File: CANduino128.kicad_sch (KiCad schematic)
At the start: 37 parts, among them J2 Conn_01x10, U1 AVR-H128-CAN, U2 74AHC373

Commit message: Mise à niveau du pin-out avec l'autre form-factor
git-svn-id: file:///D%5C00%20-%20Dev%20&%20Calculs%5CRepoTortoiseSVN_PCB%5CCANduino128/branches/CANduino128%20-%20v3.x@95 67ddf66f-3787-a644-8df7-7746e21a92b3
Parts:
- removed D2, D22: MountingHole_Pad, Connector_Wire:SolderWire-0.5sqmm_1x01_D0.9mm_OD2.1mm, symbol Mechanical:MountingHole_Pad
- added J1: Conn_01x02, TerminalBlock_Phoenix:TerminalBlock_Phoenix_MPT-0,5-2-2.54_1x02_P2.54mm_Horizontal, symbol Connector_Generic:Conn_01x02
- added JP1: SolderJumper_2_Open, Jumper:SolderJumper-2_P1.3mm_Open_RoundedPad1.0x1.5mm, symbol Jumper:SolderJumper_2_Open
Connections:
- net +BATT: now also J1.2 (Pin_2); no longer J_Comm_0.8 (Pin_8)
- net ADR15: now also JP1.1 (A)
- net CANH: now also J_Comm_0.6 (Pin_6); no longer J_Comm_0.5 (Pin_5)
- net CANL: now also J_Comm_0.5 (Pin_5); no longer J_Comm_0.6 (Pin_6)
- net GND: now also J1.1 (Pin_1); no longer J_Comm_0.7 (Pin_7)
- net OC1A: now also BLDC2.1 (Pin_1); no longer BLDC2.4 (Pin_4)
- net OC1B: now also BLDC2.2 (Pin_2); no longer BLDC2.5 (Pin_5)
- net OC1C: now also BLDC2.3 (Pin_3); no longer BLDC2.6 (Pin_6)
- net PIN_PD2_INT2_RXD1: now also BLDC2.4 (Pin_4); no longer BLDC2.2 (Pin_2)
- net PIN_PD3_INT3_TXD1: now also BLDC2.5 (Pin_5); no longer BLDC2.3 (Pin_3)
- net PIN_PE6_INT6: now also BLDC1.5 (Pin_5); no longer BLDC1.4 (Pin_4)
- net PIN_PE7_INT7: now also BLDC1.6 (Pin_6); no longer BLDC1.5 (Pin_5)
- net SCL_INT0: now also J_Comm_0.7 (Pin_7); no longer BLDC1.6 (Pin_6)
- net SDA_INT1: now also J_Comm_0.8 (Pin_8); no longer BLDC2.1 (Pin_1)
- net T0_OC0x: now also BusISA8.20 (BCLK); no longer BusISA8.30 (OSC)
- net PIN_PE2: now reaches U1.4 (PE2-D2-AIN0)
- net PIN_PE2: now also BLDC1.4 (Pin_4)
- net ICP1 renamed PIN_PD4
- net PIN_PD4: now also BLDC2.6 (Pin_6); no longer BusISA8.20 (BCLK)
- net SysClk renamed SW_Clock
- new net CPU_CLCK: BusISA8.30 (OSC), JP1.2 (B)
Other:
- moved on the sheet: BLDC2, CAN_RX_1, D25, KiCad0, OpenHW1, Pad_SCL1, Pad_SDA1, R_SCL1, R_SDA1

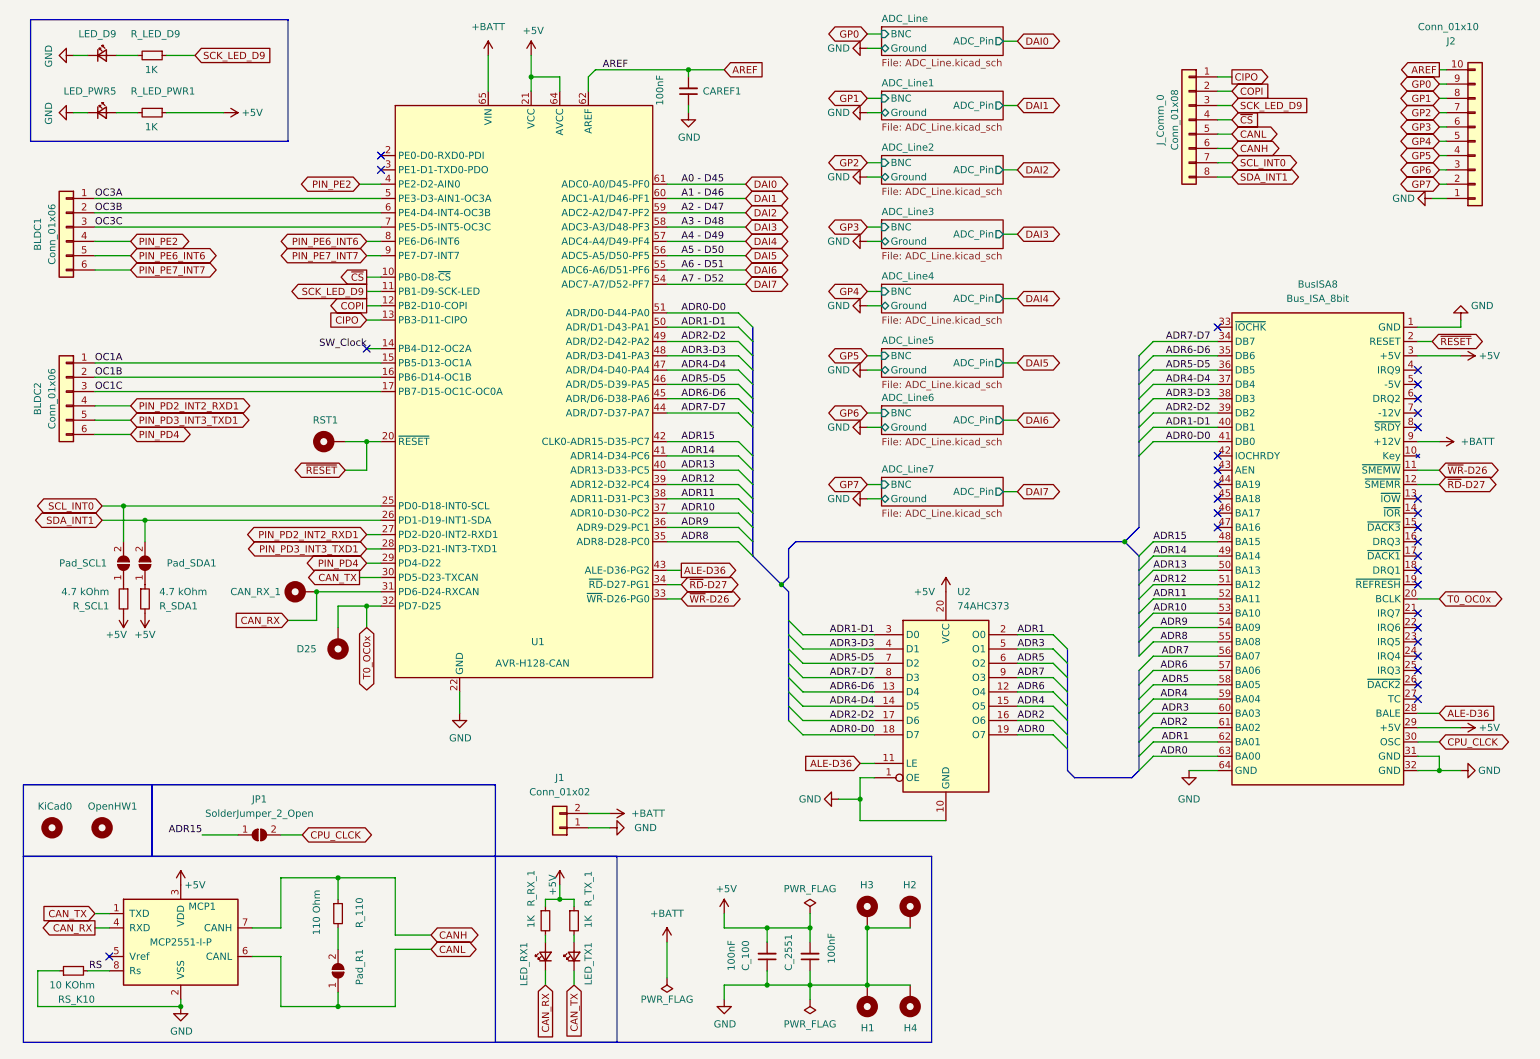
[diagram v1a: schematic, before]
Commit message: Houlà y'a eu du taf ! - fin MAJ pin-out iso v4.0a - ajout demux CD4555 pour lignes DRQ1/2/3 sur le connecteur ISA8 - pifiou ! les modifs de routages
git-svn-id: file:///D%5C00%20-%20Dev%20&%20Calculs%5CRepoTortoiseSVN_PCB%5CCANduino128/branches/CANduino128%20-%20v3.x@96 67ddf66f-3787-a644-8df7-7746e21a92b3
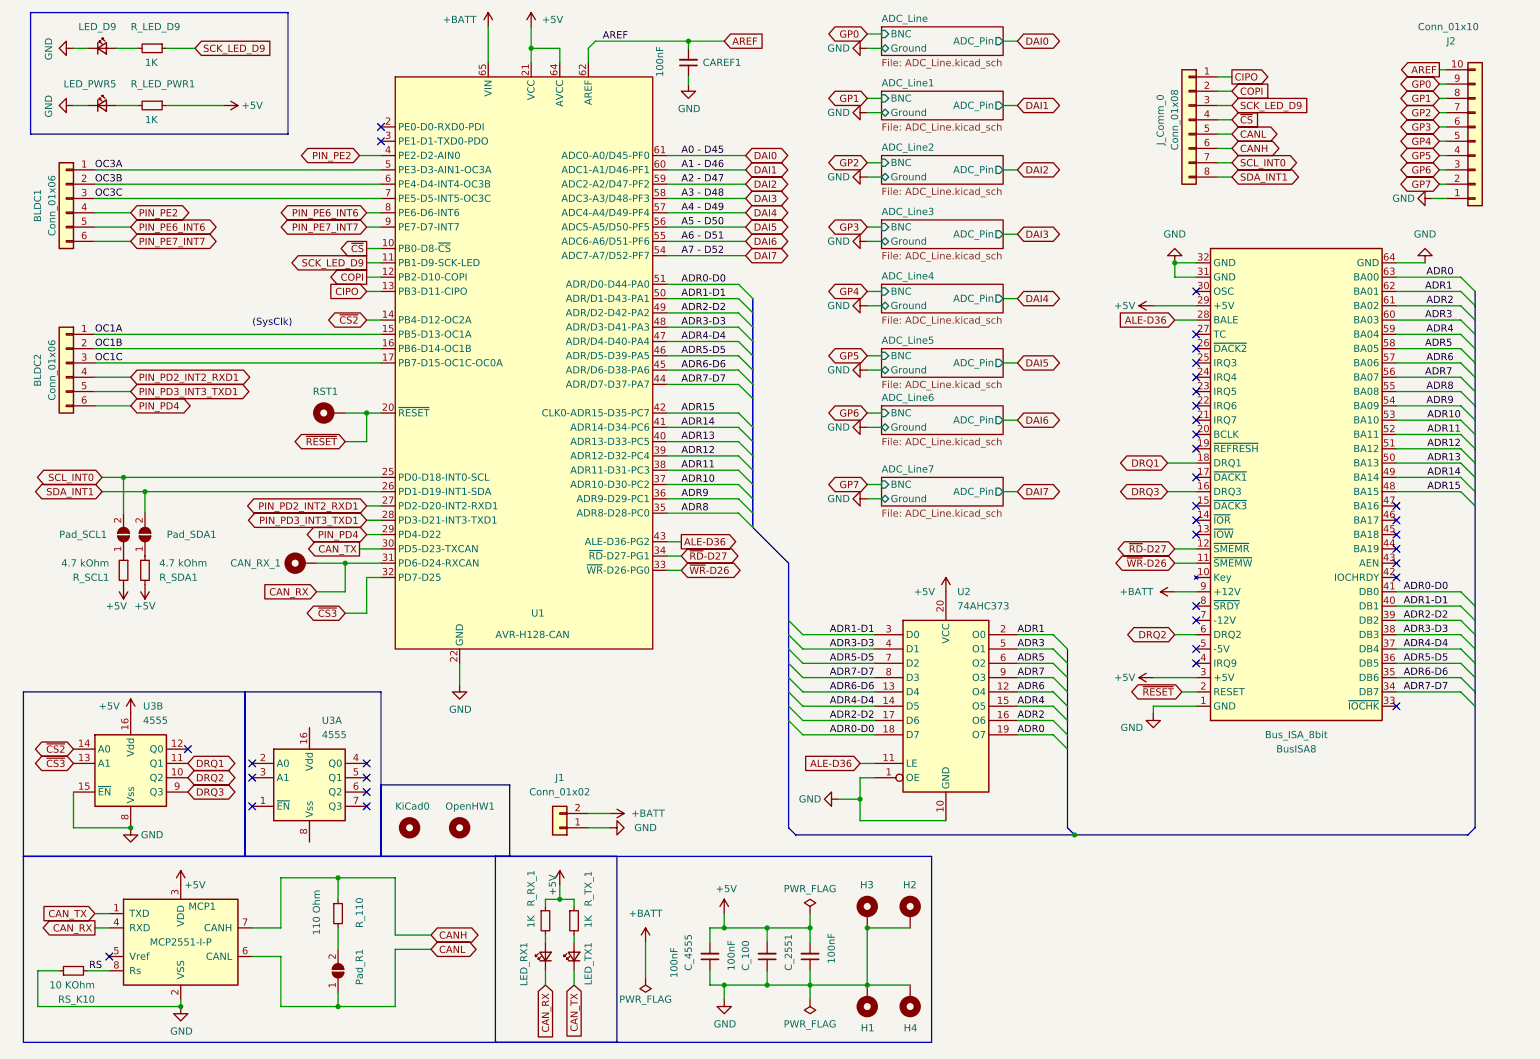
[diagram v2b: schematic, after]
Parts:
- removed D25: MountingHole_Pad, Connector_Wire:SolderWire-0.5sqmm_1x01_D0.9mm_OD2.1mm, symbol Mechanical:MountingHole_Pad
- removed JP1: SolderJumper_2_Open, Jumper:SolderJumper-2_P1.3mm_Open_RoundedPad1.0x1.5mm, symbol Jumper:SolderJumper_2_Open
- added C_4555: 100nF, Capacitor_SMD:C_1210_3225Metric_Pad1.33x2.70mm_HandSolder, symbol Device:C_Small
- added U3: 4555, Package_DIP_AKL:DIP-16_W7.62mm_Socket_LongPads, symbol 4xxx_IEEE:4555
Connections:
- net +5V: now also C_4555.2, U3.16 (Vdd)
- net GND: now also C_4555.1, U3.15 (~{EN}), U3.8 (Vss)
- net DRQ3: now reaches BusISA8.16 (DRQ3)
- net DRQ3: now also U3.9 (Q3)
- net DRQ1: now reaches BusISA8.18 (DRQ1)
- net DRQ1: now also U3.11 (Q1)
- net DRQ2: now reaches BusISA8.6 (DRQ2)
- net DRQ2: now also U3.10 (Q2)
- net CPU_CLCK: no longer names the net of BusISA8.30 (OSC)
- net SW_Clock renamed ~{CS2}
- net ~{CS2}: now also U3.14 (A0)
- net T0_OC0x: no longer names the net of BusISA8.20 (BCLK)
- net T0_OC0x: no longer U1.32 (PD7-D25)
- new net ~{CS3}: U1.32 (PD7-D25), U3.13 (A1)
- no-connect marks 30 -> 36
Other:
- note added: "(SysClk)"
- moved on the sheet: BLDC1, BLDC2, BusISA8, CAN_RX_1, CAREF1, KiCad0, LED_D9, LED_PWR5, OpenHW1, Pad_SCL1, Pad_SDA1, RST1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

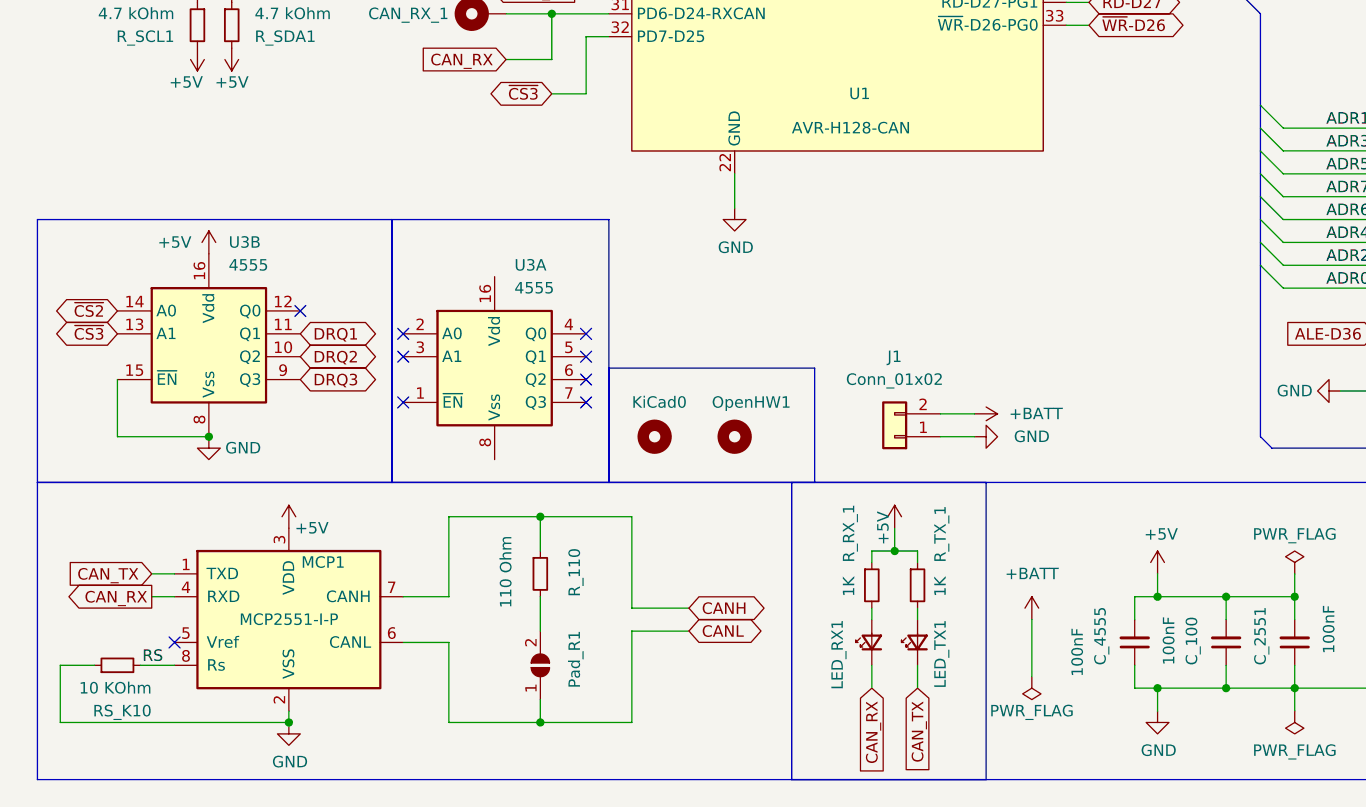
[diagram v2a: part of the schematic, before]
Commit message: YES ! On a réussi à les câbler en /CS2 et /CS3 comme des chip select de la V4.0a
git-svn-id: file:///D%5C00%20-%20Dev%20&%20Calculs%5CRepoTortoiseSVN_PCB%5CCANduino128/branches/CANduino128%20-%20v3.x@97 67ddf66f-3787-a644-8df7-7746e21a92b3
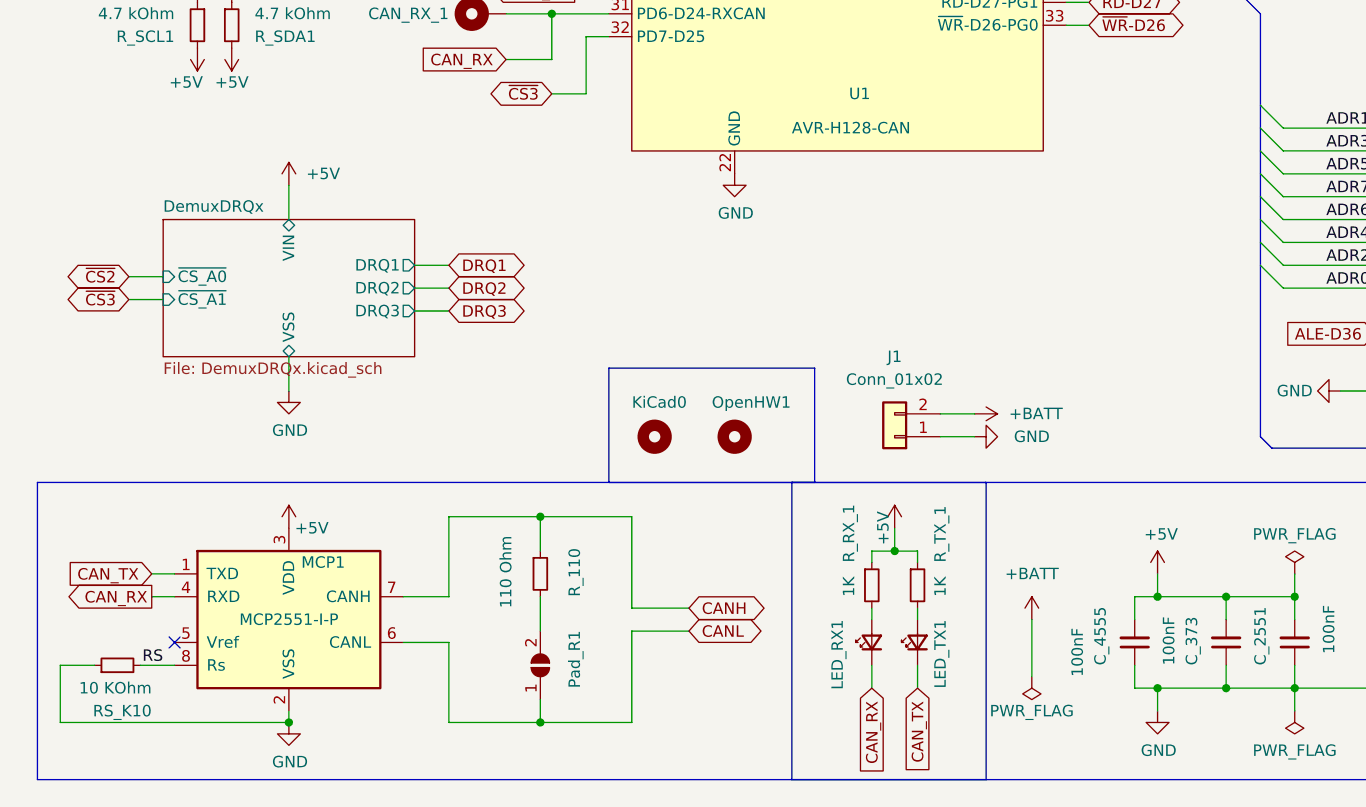
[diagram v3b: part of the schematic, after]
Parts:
- removed U3: 4555, Package_DIP_AKL:DIP-16_W7.62mm_Socket_LongPads, symbol 4xxx_IEEE:4555
- renumbered C_100 to C_373
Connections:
- no-connect marks 36 -> 28
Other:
- added sheet DemuxDRQx (DemuxDRQx.kicad_sch)
